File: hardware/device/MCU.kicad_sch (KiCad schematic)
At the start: 25 parts, among them SW24 NRST, U1 BMDU, U18 STM32H743ZIT6

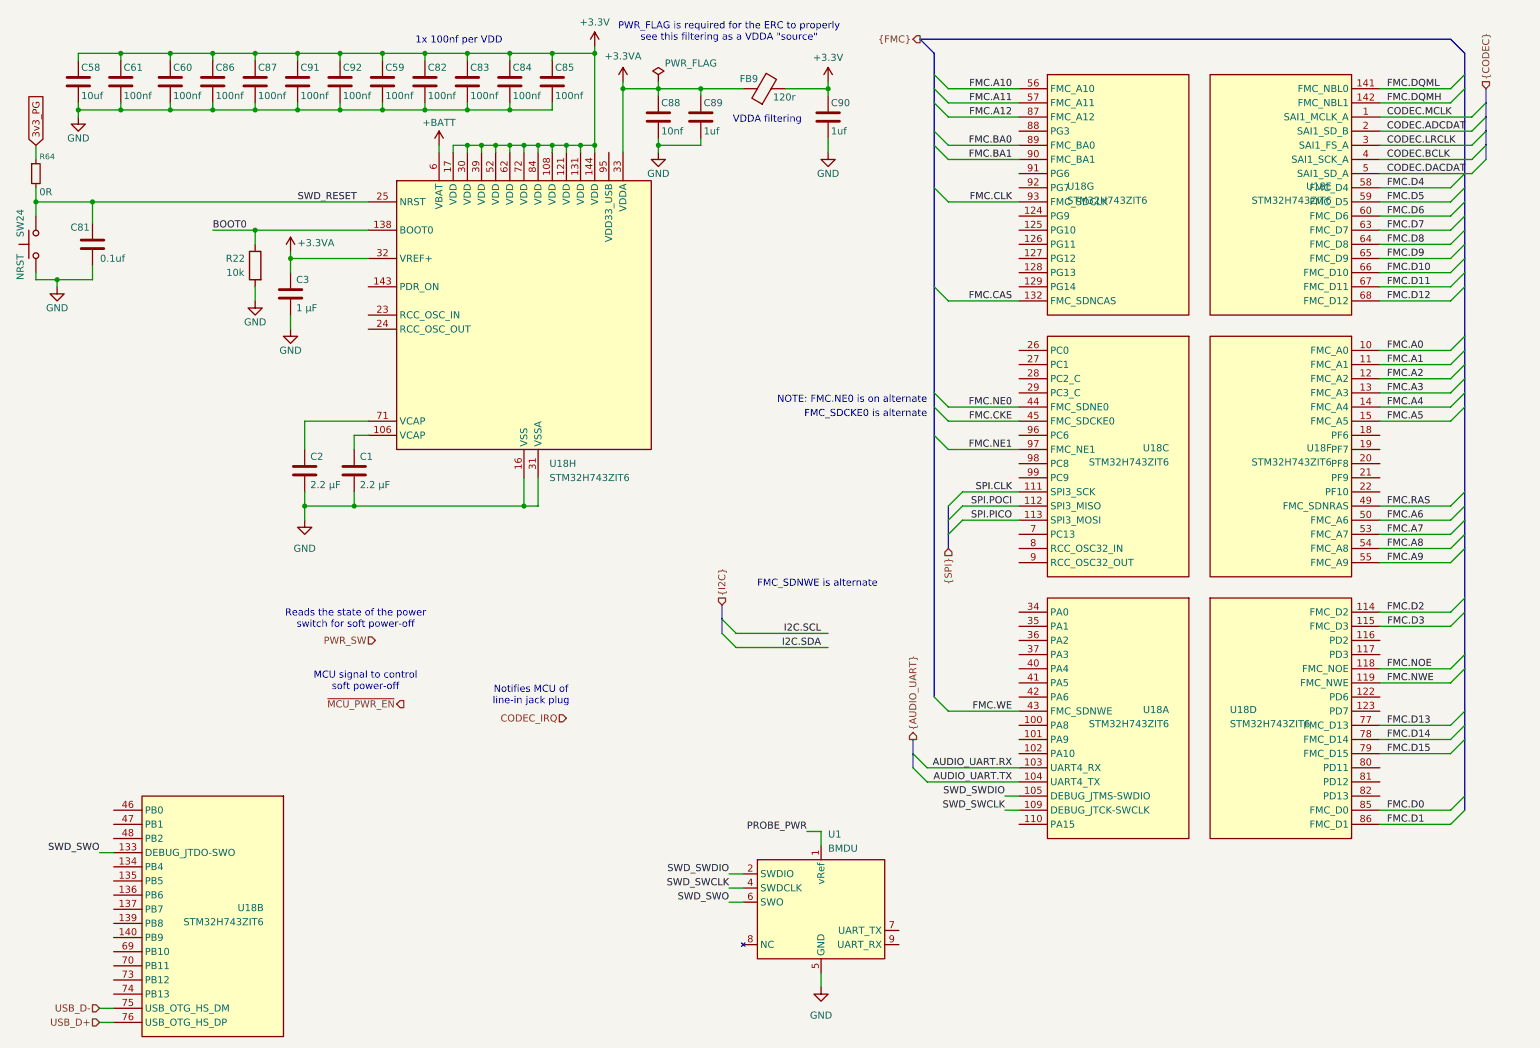
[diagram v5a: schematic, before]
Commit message: feat: various layout, start adding capacitive pads
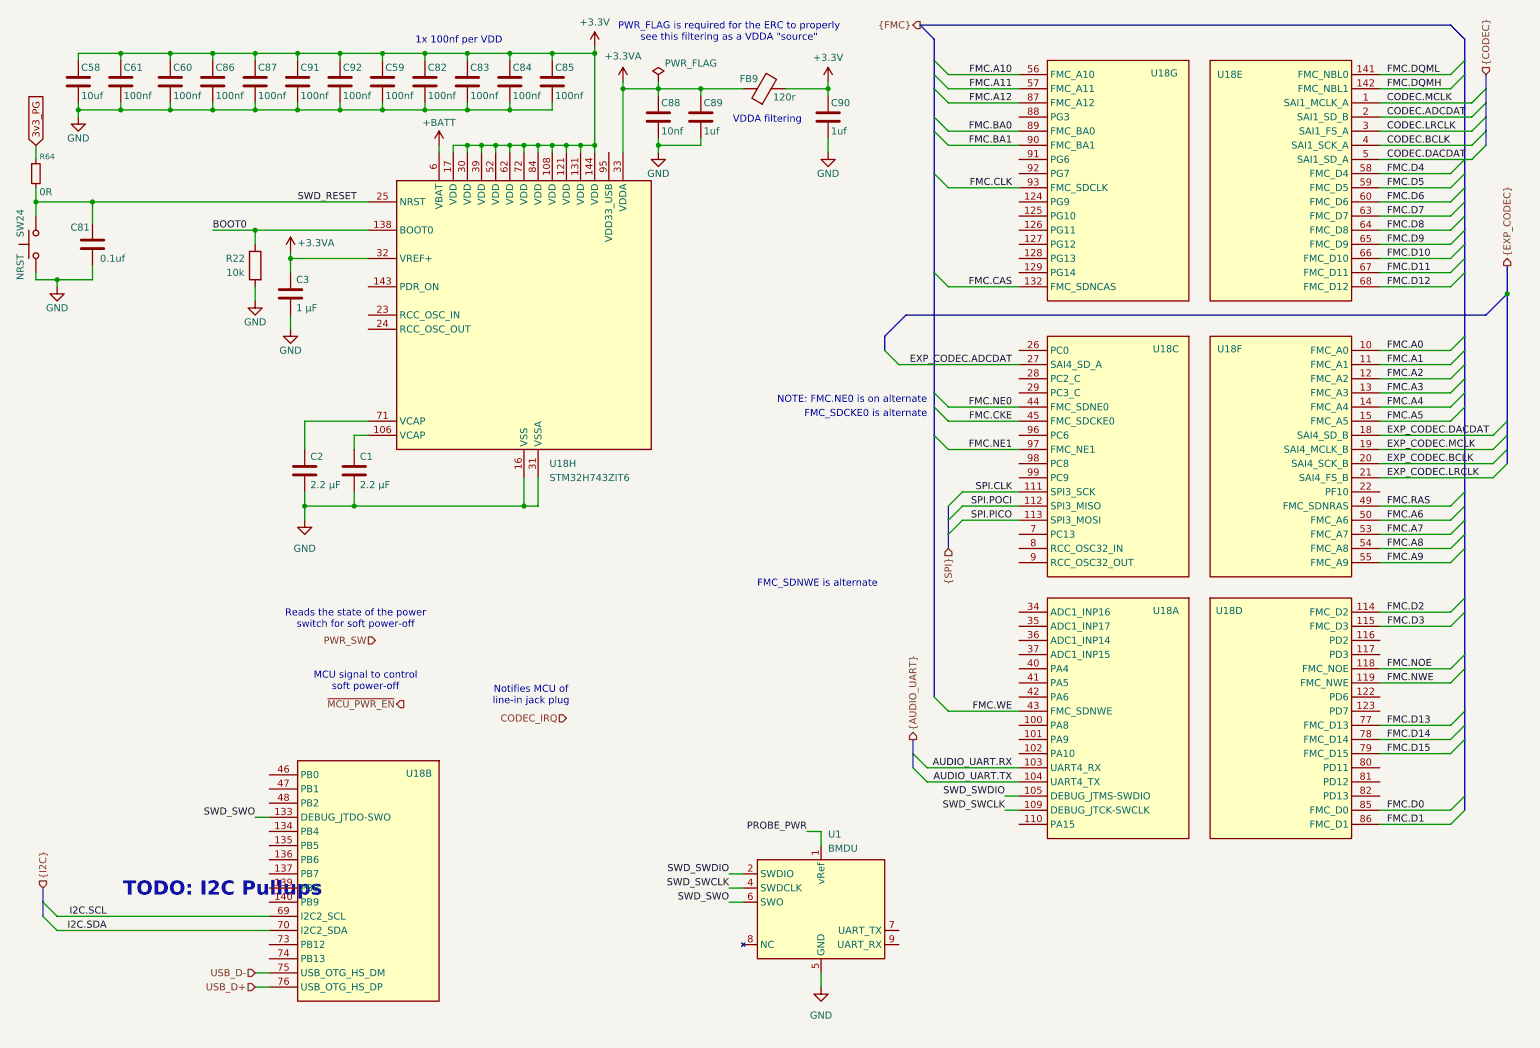
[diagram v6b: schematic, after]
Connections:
- net I2C.SCL: now also U18.69 (PB10)
- net I2C.SDA: now also U18.70 (PB11)
- net EXP_CODEC.DACDAT: now reaches U18.18 (PF6)
- net EXP_CODEC.MCLK: now reaches U18.19 (PF7)
- net EXP_CODEC.BCLK: now reaches U18.20 (PF8)
- net EXP_CODEC.LRCLK: now reaches U18.21 (PF9)
- net EXP_CODEC.ADCDAT: now reaches U18.27 (PC1)
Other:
- note added: "TODO: I2C Pullups"
- moved on the sheet: U18B, U18E, U18G

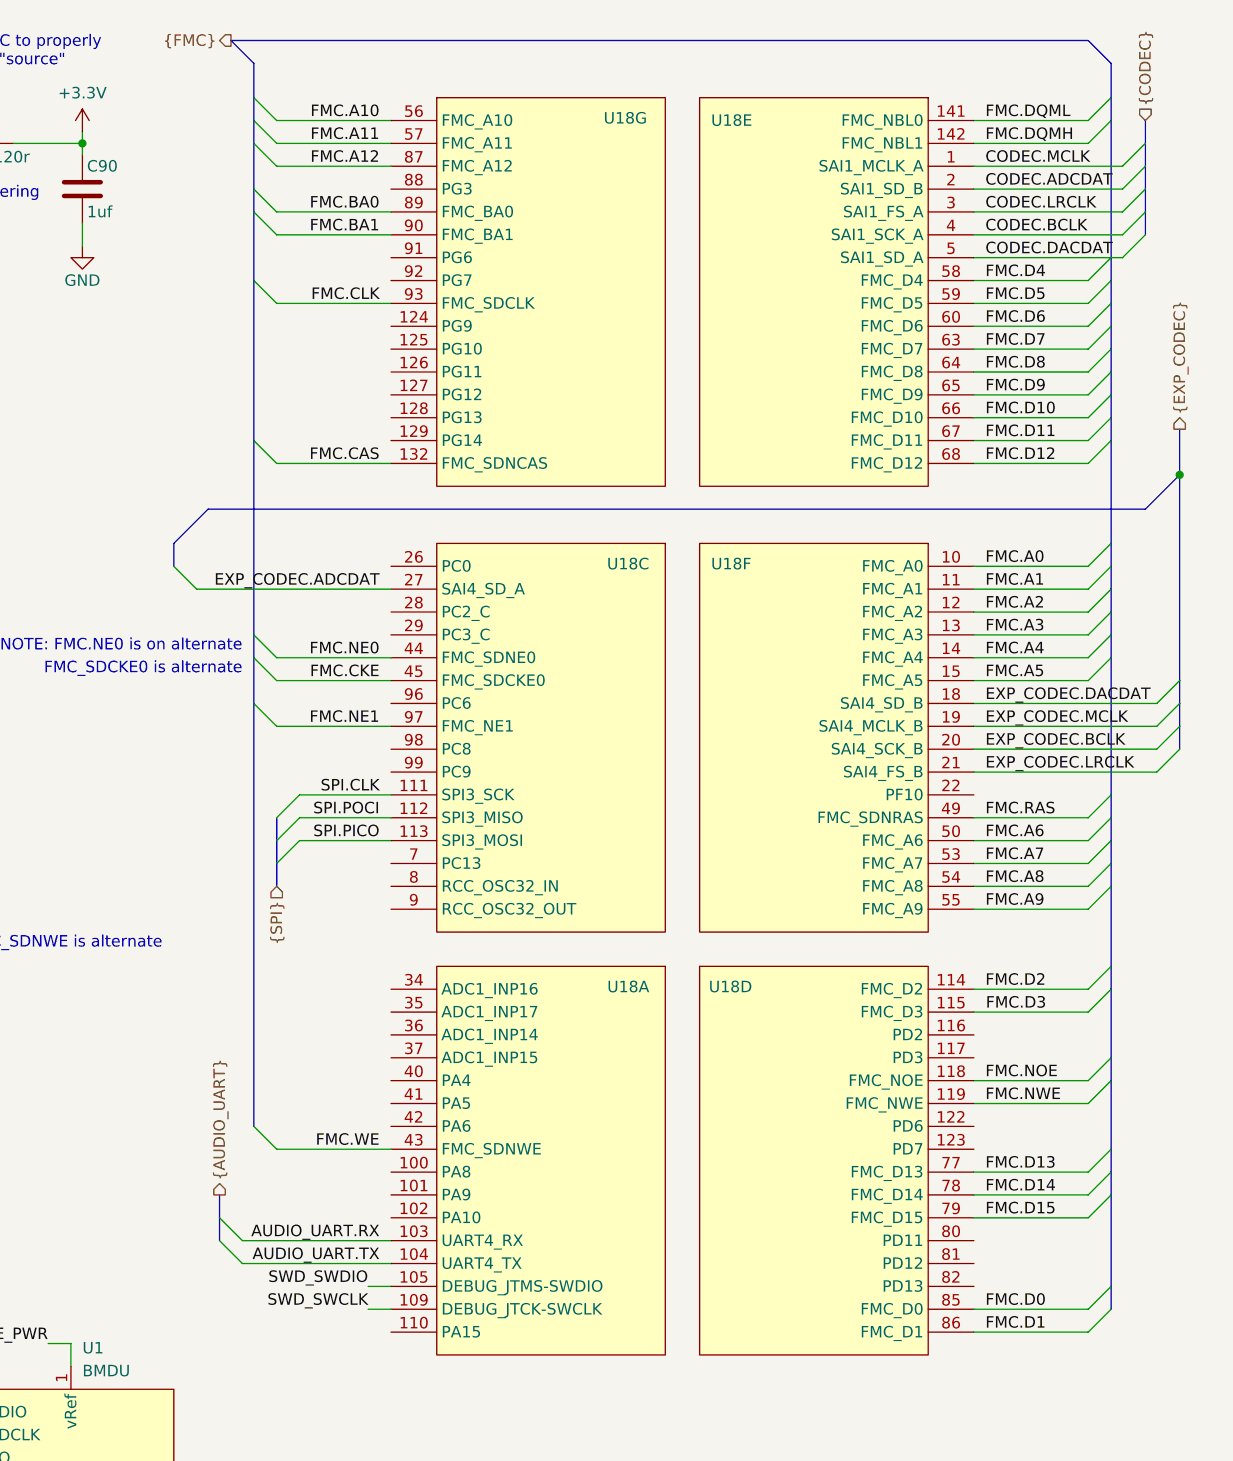
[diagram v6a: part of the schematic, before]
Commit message: feat: add integrated flash memory
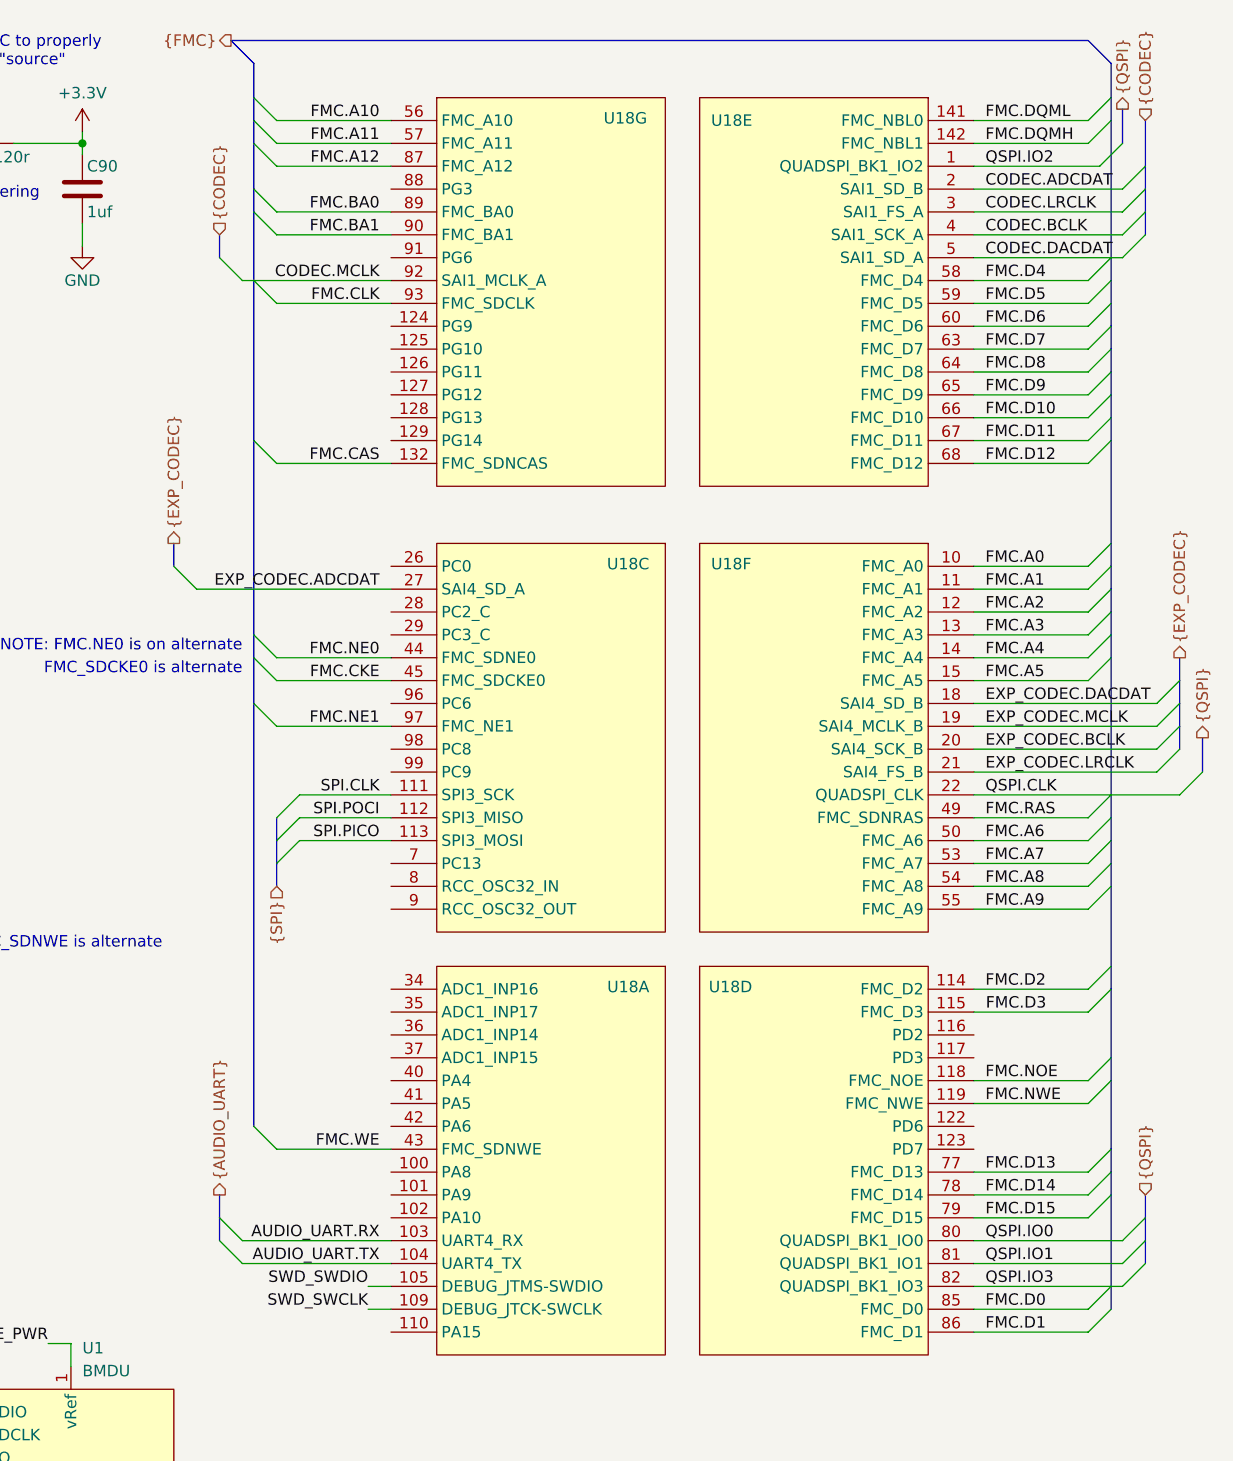
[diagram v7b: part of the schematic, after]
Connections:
- net CODEC.MCLK: now also U18.92 (PG7); no longer U18.1 (PE2)
- net QSPI.IO0: now reaches U18.80 (PD11)
- net QSPI.IO1: now reaches U18.81 (PD12)
- net QSPI.IO3: now reaches U18.82 (PD13)
- net QSPI.CLK: now reaches U18.22 (PF10)
- new net QSPI.IO2: U18.1 (PE2)

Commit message: feat: add ESD filter
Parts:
- added SW25: BOOT0, Button_Switch_SMD:SW_SPST_B3U-1000P, symbol Switch:SW_Push
- SW24: footprint (none) -> Button_Switch_SMD:SW_SPST_B3U-1000P
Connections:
- net +3.3V: now also SW25.1
- net AUDIO_UART.RX: now also U18.35 (PA1); no longer U18.103 (PA11)
- net AUDIO_UART.TX: now also U18.34 (PA0); no longer U18.104 (PA12)
- net BOOT0: now also SW25.2
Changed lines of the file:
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@@
 	)
 	(bus_entry
-		(at 176.53 147.32)
+		(at 176.53 121.92)
 		(size 2.54 2.54)
 		(stroke
@@
 	)
 	(bus_entry
-		(at 179.07 152.4)
+		(at 179.07 121.92)
 		(size -2.54 -2.54)
 		(stroke
@@
 	(bus
 		(pts
-			(xy 176.53 147.32) (xy 176.53 149.86)
-		)
-		(stroke
-			(width 0)
-			(type default)
-		)
-	)
-	(bus
-		(pts
-			(xy 176.53 144.78) (xy 176.53 147.32)
+			(xy 176.53 119.38) (xy 176.53 121.92)
 		)
 		(stroke
@@
 	(wire
 		(pts
+			(xy 24.13 78.74) (xy 19.05 78.74)
+		)
+		(stroke
+			(width 0)
+			(type default)
+		)
+	)
+	(wire
+		(pts
 			(xy 161.29 36.83) (xy 161.29 39.37)
 		)
@@
 		)
 	)
+	(bus
+		(pts
+			(xy 176.53 116.84) (xy 176.53 119.38)
+		)
+		(stroke
+			(width 0)
+			(type default)
+		)
+	)
 	(wire
 		(pts
@@
 	(wire
 		(pts
+			(xy 34.29 78.74) (xy 36.83 78.74)
+		)
+		(stroke
+			(width 0)
+			(type default)
+		)
+	)
+	(wire
+		(pts
 			(xy 138.43 36.83) (xy 138.43 38.1)
 		)
@@
 	(wire
 		(pts
-			(xy 179.07 152.4) (xy 195.58 152.4)
+			(xy 179.07 121.92) (xy 195.58 121.92)
 		)
 		(stroke
@@
 	(wire
 		(pts
-			(xy 50.8 53.34) (xy 58.42 53.34)
+			(xy 55.88 53.34) (xy 58.42 53.34)
 		)
 		(stroke
@@
 	(wire
 		(pts
-			(xy 179.07 149.86) (xy 195.58 149.86)
+			(xy 179.07 124.46) (xy 195.58 124.46)
 		)
 		(stroke
@@
 		)
 	)
+	(wire
+		(pts
+			(xy 19.05 76.2) (xy 19.05 78.74)
+		)
+		(stroke
+			(width 0)
+			(type default)
+		)
+	)
 	(bus
 		(pts
@@
 	)
 	(label "AUDIO_UART.RX"
-		(at 194.31 149.86 180)
+		(at 194.31 124.46 180)
 		(effects
 			(font
@@
 	)
 	(label "AUDIO_UART.TX"
-		(at 194.31 152.4 180)
+		(at 194.31 121.92 180)
 		(effects
 			(font
@@
 		)
 	)
+	(label "BOOT0"
+		(at 36.83 78.74 0)
+		(effects
+			(font
+				(size 1.27 1.27)
+			)
+			(justify left bottom)
+		)
+	)
 	(label "EXP_CODEC.LRCLK"
 		(at 261.62 97.79 0)
@@
 	)
 	(label "BOOT0"
-		(at 50.8 53.34 0)
+		(at 55.88 53.34 180)
 		(effects
 			(font
 				(size 1.27 1.27)
 			)
-			(justify left bottom)
+			(justify right bottom)
 		)
 	)
@@
 	(hierarchical_label "{AUDIO_UART}"
 		(shape output)
-		(at 176.53 144.78 90)
+		(at 176.53 116.84 90)
 		(effects
 			(font
@@
 	)
 	(symbol
+		(lib_id "power:+3.3V")
+		(at 19.05 76.2 0)
+		(unit 1)
+		(exclude_from_sim no)
+		(in_bom yes)
+		(on_board yes)
+		(dnp no)
+		(property "Reference" "#PWR0126"
+			(at 19.05 80.01 0)
+			(effects
+				(font
+					(size 1.27 1.27)
+				)
+				(hide yes)
+			)
+		)
+		(property "Value" "+3.3V"
+			(at 19.05 71.882 0)
+			(effects
+				(font
+					(size 1.27 1.27)
+				)
+			)
+		)
+		(property "Footprint" ""
+			(at 19.05 76.2 0)
+			(effects
+				(font
+					(size 1.27 1.27)
+				)
+				(hide yes)
+			)
+		)
+		(property "Datasheet" ""
+			(at 19.05 76.2 0)
+			(effects
+				(font
+					(size 1.27 1.27)
+				)
+				(hide yes)
+			)
+		)
+		(property "Description" "Power symbol creates a global label with name \"+3.3V\""
+			(at 19.05 76.2 0)
+			(effects
+				(font
+					(size 1.27 1.27)
+				)
+				(hide yes)
+			)
+		)
+		(pin "1"
+		)
+		(instances
+			(project "pocket_synth"
+				(path "/485383b8-00f4-4405-b270-de249939cff4/0f59ca20-5500-4399-8ffa-55aebf6eb4ee"
+					(reference "#PWR0126")
+					(unit 1)
+				)
+			)
+		)
+	)
+	(symbol
 		(lib_id "Switch:SW_Push")
 		(at 19.05 55.88 90)
@@
 			)
 		)
-		(property "Footprint" ""
+		(property "Footprint" "Button_Switch_SMD:SW_SPST_B3U-1000P"
 			(at 13.97 55.88 0)
 			(effects
@@
 	)
 	(symbol
+		(lib_id "Switch:SW_Push")
+		(at 29.21 78.74 0)
+		(unit 1)
+		(exclude_from_sim no)
+		(in_bom yes)
+		(on_board yes)
+		(dnp no)
+		(property "Reference" "SW25"
+			(at 33.02 75.946 0)
+			(effects
+				(font
+					(size 1.27 1.27)
+				)
+			)
+		)
+		(property "Value" "BOOT0"
+			(at 25.146 75.946 0)
+			(effects
+				(font
+					(size 1.27 1.27)
+				)
+			)
+		)
+		(property "Footprint" "Button_Switch_SMD:SW_SPST_B3U-1000P"
+			(at 29.21 73.66 0)
+			(effects
+				(font
+					(size 1.27 1.27)
+				)
+				(hide yes)
+			)
+		)
+		(property "Datasheet" "~"
+			(at 29.21 73.66 0)
+			(effects
+				(font
+					(size 1.27 1.27)
+				)
+				(hide yes)
+			)
+		)
+		(property "Description" "Push button switch, generic, two pins"
+			(at 29.21 78.74 0)
+			(effects
+				(font
+					(size 1.27 1.27)
+				)
+				(hide yes)
+			)
+		)
+		(property "Height" ""
+			(at 29.21 78.74 0)
+			(effects
+				(font
+					(size 1.27 1.27)
+				)
+			)
+		)
+		(property "Manufacturer_Name" ""
+			(at 29.21 78.74 0)
+			(effects
+				(font
+					(size 1.27 1.27)
+				)
+			)
+		)
+		(property "Manufacturer_Part_Number" ""
+			(at 29.21 78.74 0)
+			(effects
+				(font
+					(size 1.27 1.27)
+				)
+			)
+		)
+		(property "Mouser Part Number" ""
+			(at 29.21 78.74 0)
+			(effects
+				(font
+					(size 1.27 1.27)
+				)
+			)
+		)
+		(property "Mouser Price/Stock" ""
+			(at 29.21 78.74 0)
+			(effects
+				(font
+					(size 1.27 1.27)
+				)
+			)
+		)
+		(pin "2"
+		)
+		(pin "1"
+		)
+		(instances
+			(project "pocket_synth"
+				(path "/485383b8-00f4-4405-b270-de249939cff4/0f59ca20-5500-4399-8ffa-55aebf6eb4ee"
+					(reference "SW25")
+					(unit 1)
+				)
+			)
+		)
+	)
+	(symbol
 		(lib_id "power:+3.3V")
 		(at 161.29 26.67 0)
@@
 		)
 		(pin "34"
-			(alternate "ADC1_INP16")
+			(alternate "UART4_TX")
 		)
 		(pin "35"
-			(alternate "ADC1_INP17")
+			(alternate "UART4_RX")
 		)
 		(pin "36"
@@
 		)
 		(pin "103"
-			(alternate "UART4_RX")
+			(alternate "PA11")
 		)
 		(pin "104"
-			(alternate "UART4_TX")
+			(alternate "PA12")
 		)
 		(pin "105"
